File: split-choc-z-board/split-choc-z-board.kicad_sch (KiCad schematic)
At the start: 42 parts, among them P1 USB_C_Plug, SW1 SW_SPST, SW10 SW_SPST, SW11 SW_SPST, SW12 SW_SPST, SW13 SW_SPST, SW14 SW_SPST, SW15 SW_SPST, SW16 SW_SPST, SW17 SW_SPST, SW18 SW_SPST, SW2 SW_SPST, SW3 SW_SPST, SW4 SW_SPST, SW5 SW_SPST, SW6 SW_SPST, SW7 SW_SPST, SW8 SW_SPST, SW9 SW_SPST

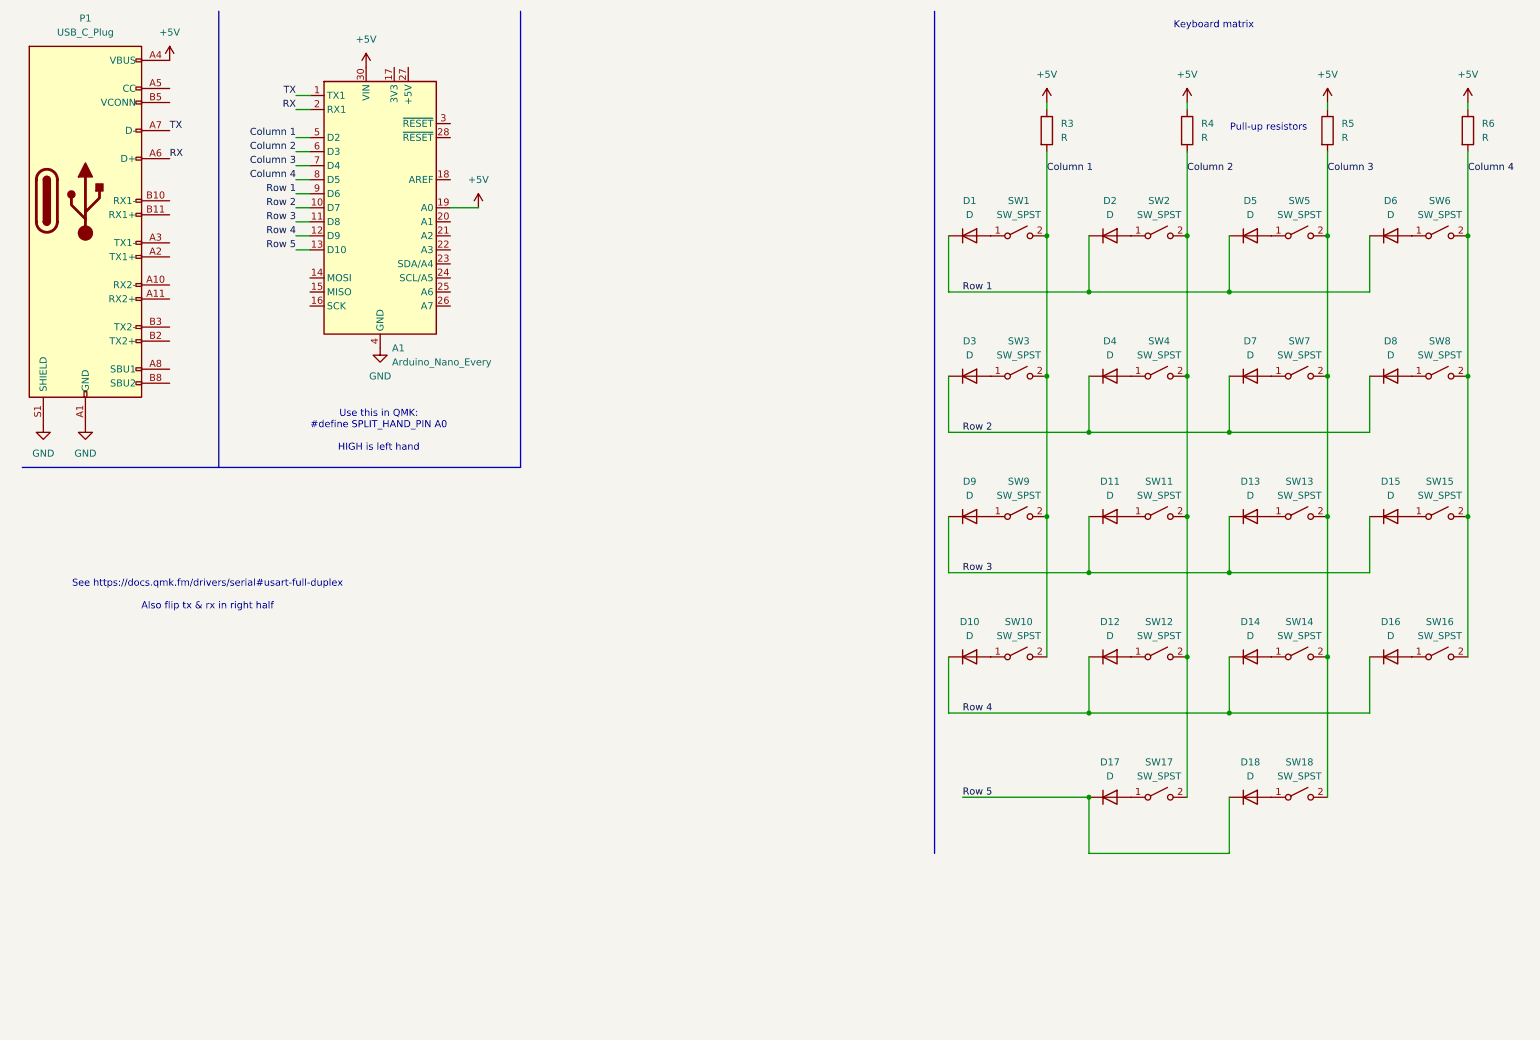
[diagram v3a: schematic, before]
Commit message: Update: Defined components in README and added ESD protection. Also changed USBC connector
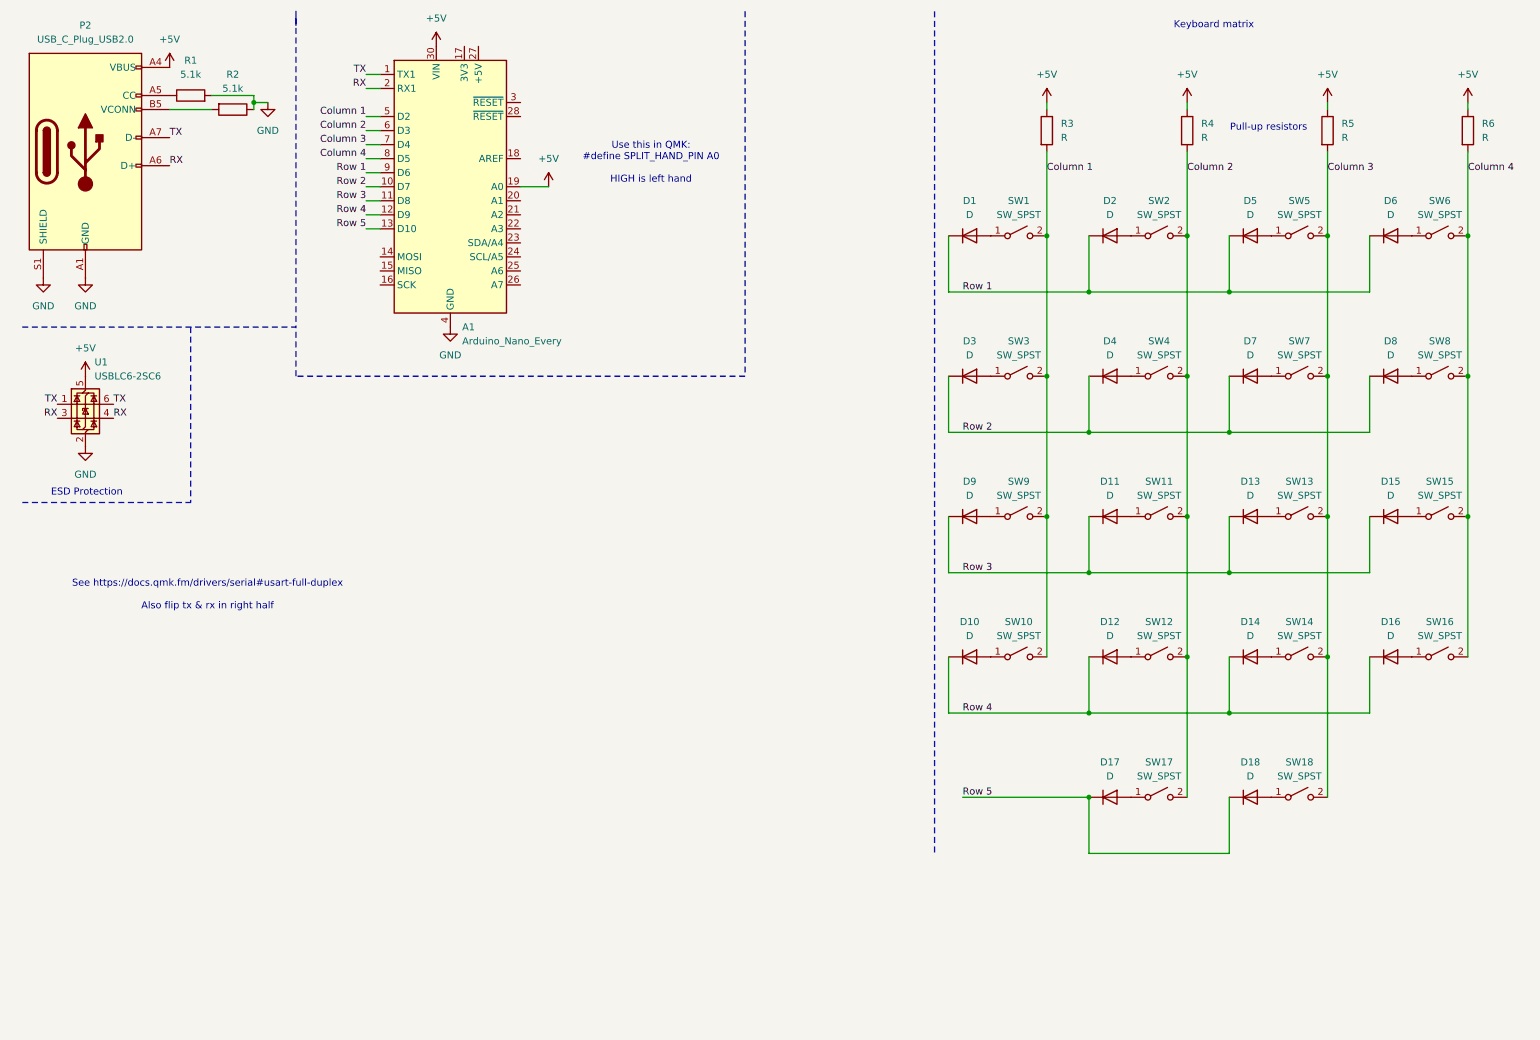
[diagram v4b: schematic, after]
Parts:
- removed P1: USB_C_Plug, symbol Connector:USB_C_Plug
- added P2: USB_C_Plug_USB2.0, symbol Connector:USB_C_Plug_USB2.0
- added R1, R2: 5.1k, symbol Device:R
- added U1: USBLC6-2SC6, Package_TO_SOT_SMD:SOT-23-6, symbol Power_Protection:USBLC6-2SC6
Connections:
- net +5V: now also P2.A4 (VBUS), P2.A9 (VBUS), P2.B4 (VBUS), P2.B9 (VBUS), U1.5 (VBUS)
- net GND: now also P2.A1 (GND), P2.A12 (GND), P2.B1 (GND), P2.B12 (GND), P2.S1 (SHIELD), R1.2, R2.1, U1.2 (GND)
- net RX: now also P2.A6 (D+), U1.3 (I/O2), U1.4 (I/O2)
- net TX: now also P2.A7 (D-), U1.1 (I/O1), U1.6 (I/O1)
- new net: P2.A5 (CC), R1.1
- new net: P2.B5 (VCONN), R2.2
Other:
- note added: "ESD Protection"
- moved on the sheet: A1

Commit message: Update: Added more footprints 🚀
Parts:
- removed P2: USB_C_Plug_USB2.0, symbol Connector:USB_C_Plug_USB2.0
- added J1: USB4105-GF-A, Library:GCT_USB4105-GF-A, symbol USB4105-GF-A:USB4105-GF-A
- D1, D10, D11, D12, D13, D14, D15, D16, D17, D18, D2, D3, D4, D5, D6, D7, D8, D9: footprint Diode_THT:D_DO-35_SOD27_P7.62mm_Horizontal -> footprints:SOD123_MCC
- R1, R2: footprint (none) -> Resistor_THT:R_Axial_DIN0207_L6.3mm_D2.5mm_P10.16mm_Horizontal
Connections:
- net +5V: now also J1.A4_B9 (VBUS), J1.B4_A9 (VBUS__1)
- net GND: now also R1.1, R2.2, J1.A1_B12 (GND), J1.B1_A12 (GND__1), J1.SH1 (SHELL_GND), J1.SH2 (SHELL_GND__1), J1.SH3 (SHELL_GND__2), J1.SH4 (SHELL_GND__3); no longer R1.2, R2.1
- net RX: now also J1.B6 (DP2), J1.B7 (DN2)
- net TX: now also J1.A6 (DP1), J1.A7 (DN1)
- new net CC1: J1.A5 (CC1), R1.2
- new net CC2: J1.B5 (CC2), R2.1
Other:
- moved on the sheet: R1, R2

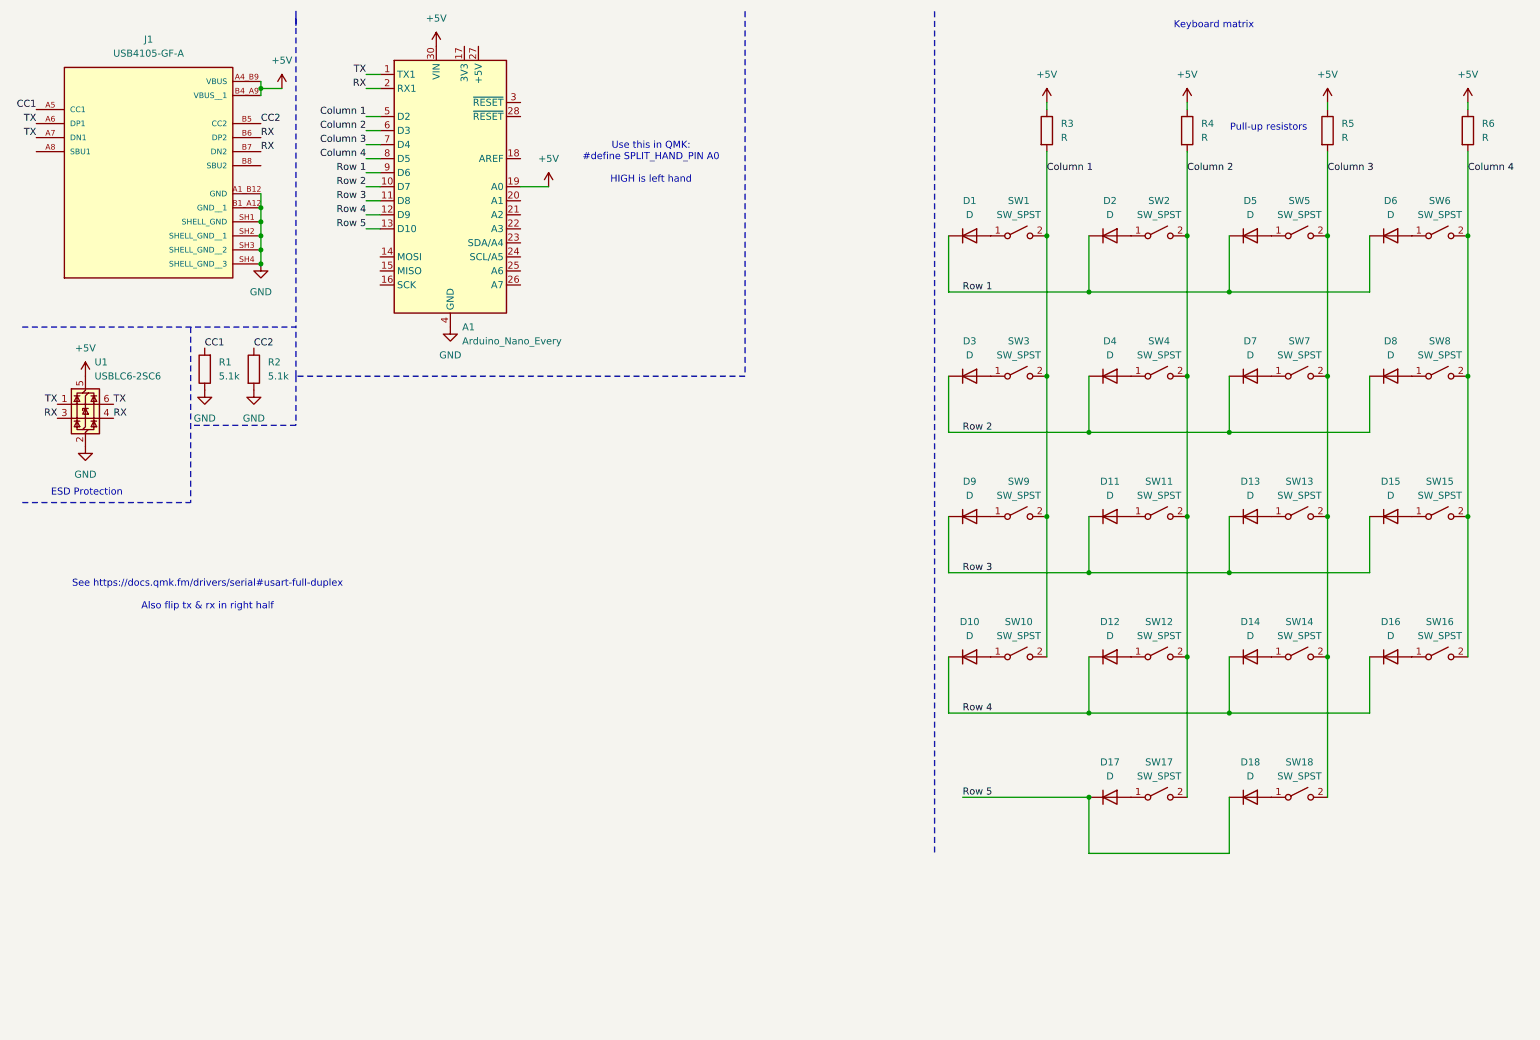
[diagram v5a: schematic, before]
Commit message: Added kb library for 128x32 oled display and deleted MCU 🥳
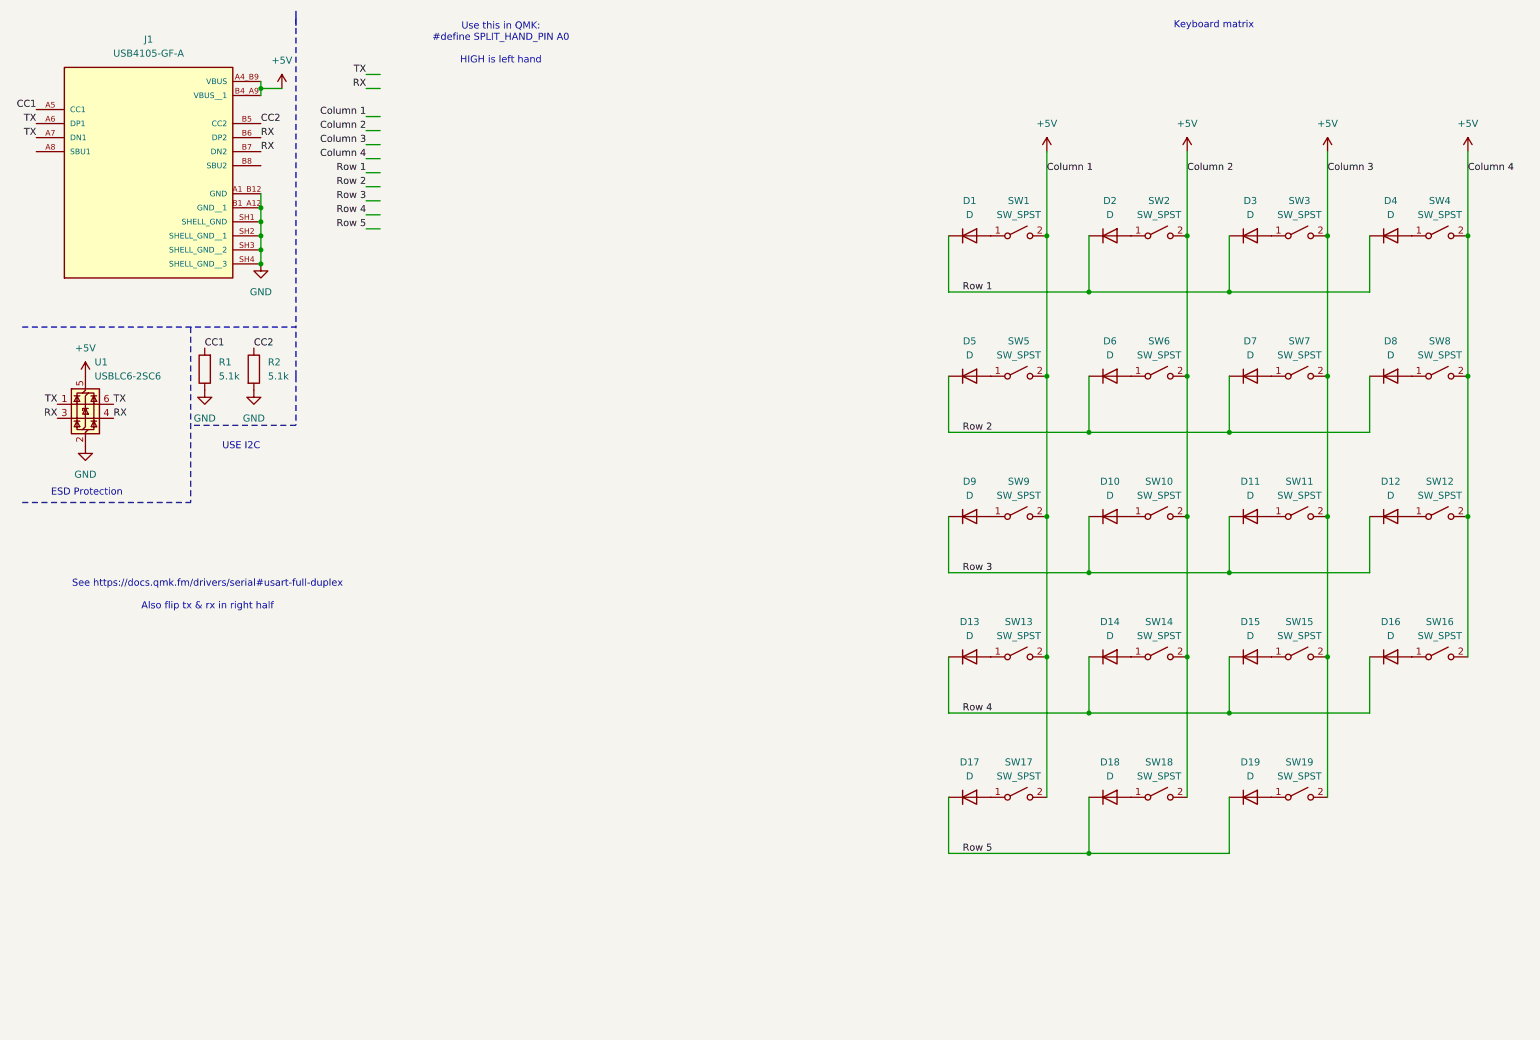
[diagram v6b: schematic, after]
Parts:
- removed A1: Arduino_Nano_Every, Module:Arduino_Nano, symbol MCU_Module:Arduino_Nano_Every
- removed R3, R4, R5, R6: R, Resistor_THT:R_Axial_DIN0207_L6.3mm_D2.5mm_P10.16mm_Horizontal, symbol Device:R
- added D17: D, footprints:SOD123_MCC, symbol Device:D
- added SW17: SW_SPST, ScottoKeebs_Choc:Choc_V2_1.00u, symbol Switch:SW_SPST
- renumbered D11 to D10, D13 to D11, D15 to D12, D10 to D13, D12 to D14, D14 to D15, D17 to D18, D18 to D19, D5 to D3, D6 to D4, D3 to D5, D4 to D6, SW11 to SW10, SW13 to SW11, SW15 to SW12, SW10 to SW13, SW12 to SW14, SW14 to SW15, SW17 to SW18, SW18 to SW19, SW5 to SW3, SW6 to SW4, SW3 to SW5, SW4 to SW6
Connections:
- net Column 1 is gone; now on net +5V: SW1.2 (B), SW13.2 (B), SW5.2 (B), SW9.2 (B)
- net Column 2 is gone; now on net +5V: SW10.2 (B), SW14.2 (B), SW18.2 (B), SW2.2 (B), SW6.2 (B)
- net Column 3 is gone; now on net +5V: SW11.2 (B), SW15.2 (B), SW19.2 (B), SW3.2 (B), SW7.2 (B)
- net Column 4 is gone; now on net +5V: SW12.2 (B), SW16.2 (B), SW4.2 (B), SW8.2 (B)
- net +5V: now also SW17.2 (B)
- net Row 5: now also D17.1 (K)
- new net: D17.2 (A), SW17.1 (A)
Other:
- note added: "USE I2C"
- note removed: "Pull-up resistors"

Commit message: Added RP2040! 😅 Hopefully no errors to come
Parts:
- added C1, C4: 1u, Capacitor_SMD:C_0402_1005Metric, symbol Device:C
- added C10, C11, C14, C2, C3, C5, C6, C7, C8, C9: 100n, Capacitor_SMD:C_0402_1005Metric, symbol Device:C
- added C12, C13: 10u, Capacitor_SMD:C_0402_1005Metric, symbol Device:C
- added C15, C16: 15p, Capacitor_SMD:C_0402_1005Metric, symbol Device:C
- added D20: D, footprints:SOD123_MCC, symbol Device:D
- added J2: USB4105-GF-A, Library:GCT_USB4105-GF-A, symbol USB4105-GF-A:USB4105-GF-A
- added R3, R4: 27.4, Resistor_SMD:R_0603_1608Metric, symbol Device:R
- added R5: 10k, Resistor_SMD:R_0603_1608Metric, symbol Device:R
- added R6, R7, R8: 1k, Resistor_SMD:R_0603_1608Metric, symbol Device:R
- added SW20: SW_SPST, ScottoKeebs_Choc:Choc_V1_1.00u, symbol Switch:SW_SPST
- added SW21, SW22: SW_SPST, symbol Switch:SW_SPST
- added U2: RP2040, Package_DFN_QFN:QFN-56-1EP_7x7mm_P0.4mm_EP3.2x3.2mm, symbol MCU_RaspberryPi:RP2040
- added U3: NCP1117-3.3_SOT223, Package_TO_SOT_SMD:SOT-223-3_TabPin2, symbol Regulator_Linear:NCP1117-3.3_SOT223
- added U4: W25Q128JVS, Package_SO:SOIC-8_5.3x5.3mm_P1.27mm, symbol Memory_Flash:W25Q128JVS
- added U5: USBLC6-2SC6, Package_TO_SOT_SMD:SOT-23-6, symbol Power_Protection:USBLC6-2SC6
- added X1: ABM8-272-T3, Library:ABM8-272-T3_ABR, symbol 2025-06-15_23-12-14:ABM8-272-T3
- R1, R2: footprint Resistor_THT:R_Axial_DIN0207_L6.3mm_D2.5mm_P10.16mm_Horizontal -> Resistor_SMD:R_0603_1608Metric
- SW1, SW10, SW11, SW12, SW13, SW14, SW15, SW16, SW17, SW18, SW19, SW2, SW3, SW4, SW5, SW6, SW7, SW8, SW9: footprint ScottoKeebs_Choc:Choc_V2_1.00u -> ScottoKeebs_Choc:Choc_V1_1.00u
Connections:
- net GND: now also C1.2, C10.2, C11.2, C12.2, C13.2, C14.2, C15.1, C16.2, C2.2, C3.2, C4.2, C5.2, C6.2, C7.2, C8.2, C9.2, J2.A1_B12 (GND), J2.B1_A12 (GND__1), J2.SH1 (SHELL_GND), J2.SH2 (SHELL_GND__1), J2.SH3 (SHELL_GND__2), J2.SH4 (SHELL_GND__3), SW21.1 (A), SW22.1 (A), U2.57 (GND), U3.1 (GND), U4.4 (GND), U5.2 (GND), X1.2, X1.4
- net +5V renamed +3V3
- net +3V3: now also C13.1, C14.1, C4.1, R5.1, SW20.2 (B), U2.1 (IOVDD), U2.10 (IOVDD), U2.22 (IOVDD), U2.33 (IOVDD), U2.42 (IOVDD), U2.43 (ADC_AVDD), U2.44 (VREG_IN), U2.48 (USB_VDD), U2.49 (IOVDD), U3.2 (VO), U4.8 (VCC); no longer J1.A4_B9 (VBUS), J1.B4_A9 (VBUS__1), U1.5 (VBUS)
- net RX renamed USB_D-
- net USB_D-: now also J1.A7 (DN1), R4.1, U5.3 (I/O2), U5.4 (I/O2); no longer J1.B6 (DP2)
- net Row 1 renamed Row_1
- net Row 2 renamed Row_2
- net Row 3 renamed Row_3
- net Row 4 renamed Row_4
- net Row 5 renamed Row_5
- net Row_5: now also D20.1 (K)
- net TX renamed USB_D+
- net USB_D+: now also J1.B6 (DP2), R3.1, U5.1 (I/O1), U5.6 (I/O1); no longer J1.A7 (DN1)
- new net: R6.1, SW21.2 (B)
- new net: R4.2, U2.46 (USB_DM)
- new net: R3.2, U2.47 (USB_DP)
- new net: D20.2 (A), SW20.1 (A)
- new net: C16.1, R7.2, X1.3
- new net: R8.1, SW22.2 (B)
- new net +1V1: C1.1, C2.1, C3.1, U2.23 (DVDD), U2.45 (VREG_VOUT), U2.50 (DVDD)
- new net +3.3V: C10.1, C11.1, C5.1, C6.1, C7.1, C8.1, C9.1
- new net B-B_D+: J2.A6 (DP1), J2.B6 (DP2)
- new net B-B_D-: J2.A7 (DN1), J2.B7 (DN2)
- new net QSPI_SCLK: U2.52 (QSPI_SCLK), U4.6 (CLK)
- new net QSPI_SD0: U2.53 (QSPI_SD0), U4.5 (DI/IO_{0})
- new net QSPI_SD1: U2.55 (QSPI_SD1), U4.2 (DO/IO_{1})
- new net QSPI_SD2: U2.54 (QSPI_SD2), U4.3 (~{WP}/IO_{2})
- new net QSPI_SD3: U2.51 (QSPI_SD3), U4.7 (~{HOLD}/~{RESET}/IO_{3})
- new net QSPI_SS: R5.2, R6.2, U2.56 (QSPI_SS), U4.1 (~{CS})
- new net RST: R8.2, U2.26 (RUN)
- new net VBUS: C12.1, J1.A4_B9 (VBUS), J1.B4_A9 (VBUS__1), J2.A4_B9 (VBUS), J2.B4_A9 (VBUS__1), U1.5 (VBUS), U3.3 (VI), U5.5 (VBUS)
- new net XIN: C15.2, U2.20 (XIN), X1.1
- new net XOUT: R7.1, U2.21 (XOUT)
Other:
- note added: "BOOT BTN"
- note added: "Board-Board communication USB-C"
- note added: "C1 should be close to pin45"
- note added: "C4 should be close to pin44"
- note added: "Clock"
- note added: "Data USB-C"
- note added: "Decoupling capacitors"
- note added: "ESD Board-Board Protection"
- note added: "Flash memory"
- note added: "Needed to properly establish 5v with any USB-C cable"
- note added: "Power"
- note added: "RST BTN"
- note added: "USB-C PD 5v"
- note removed: "See https://docs.qmk.fm/drivers/serial#usart-full-duplex Also flip tx & rx in right half"
- note removed: "USE I2C"
- moved on the sheet: D1, D10, D11, D12, D13, D14, D15, D16, D17, D18, D19, D2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
